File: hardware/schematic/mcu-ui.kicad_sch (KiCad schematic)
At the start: 25 parts, among them Q5 N MOSFET, SW1 TACT-SW, SW2 TACT-SW, U1 TCA9535, U4 ESP32-C3, U5 ST7567-12864, U6 EC11, U7 Si5351A, X1 32.768kHz-DNP

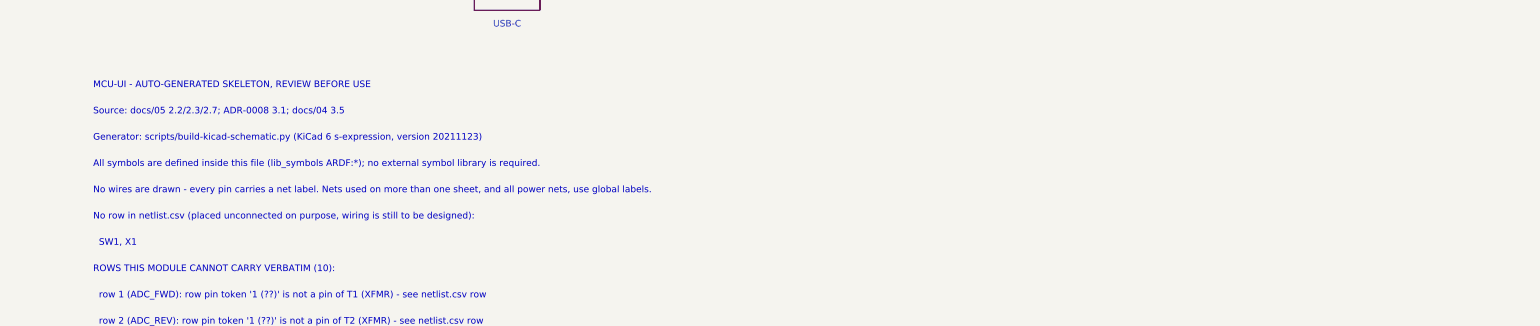
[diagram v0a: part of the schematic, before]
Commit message: docs(hw): BOM/网表生成器数据向 docs/05 同步（取消蜂鸣器 · R_BL2=100kΩ · CA-DV8008N@0x28）
前提修正: 「7 个 CSV 过期」不成立 —— 重跑后 6 个 BOM CSV + 2 个 netlist CSV
  **逐字节不变**；只有 schematic/netlist.md 变（相对 HEAD 145→123 行）
  ⇒ 真问题是「**生成器数据与 docs/05 不一致**」，重跑修不好 ⇒ 已在 3 个生成器里同步（无设计改动）

四条一致性（均已 grep 核实）:
  1. **蜂鸣器**: LS1 从「有源蜂鸣器 1 个」⇒ **本版移除 / 数量 0**; 外壳面板行同步删掉「出声孔」
  2. **R_BL2**: 10 kΩ ⇒ **100 kΩ**（BOM + netlist.md 备注）
  3. **CA-DV8008N @ 0x28**: HEAD 是 TCA9535(0x20)+ULN2003A+12V+继电器 12V 旧链
     → 现为 **U1 CA-DV8008N C54557228 / 0x28 / OC1-OC6→K1-K6 / COM→+5V / VCC→+3V3_DIG / A0-A2→GND**
     netlist 旧链 20 行只剩 1 行历史备注
  4. relay-wiring CHANGELOG 与派生文件一致（器件/地址/COM/线圈/映射/R_RLY 删除）

脚本重跑:
  · build-netlist.py → rc=0（3 产物, 155 行 / 68 nets）
  · build-lceda-import-pack.py → rc=0（9 模块 CSV + summary + bom.md）
  · **build-kicad-schematic.py → rc=1**（阻塞: netlist refs with no symbol/sheet: ['VCC','J17']）
  · check-kicad-schematic.py → **rc=1**（row coverage 181 vs netlist.csv 155）

⚠️ 未解决（已如实登记, 需设计层处理）:
  a. **KiCad 全套仍是 9/26 骨架**（含 TCA9535 / ULN2003A / U11 升压 / +12V / PA_PWR_PWM / R_RLY）
     → 需「**骨架移植**」, 重跑无法解决。**本次一个 .kicad_sch 都没写（未伪造）**, 自检器 FAIL 即为证据
  b. **GPIO 重分配未传播到生成器**（EC11_A→GPIO20 / LCD_BL→GPIO21 / GPIO12→示波器 / GPIO2→ADC1_CH2）
     生成器仍写 EC11_A=GPIO2、GPIO12_TBD、LCD_BL_DRV=TBD ⇒ 属设计数据重写（≈8 行+覆盖表）, 超出本次授权范围
  c. Q5/R_BL 的「驱动源待定」同 b（应为 GPIO21）
  d. mcu-ui.kicad_sch + kicad-build-report.md 的 10/15 改动来源不明（其余 7 份仍 9/26）

涉及: 20 个文档 .md · 3 个生成器脚本（数据同步, 无设计改动）· 11 个派生文件
  · 3 个新增: docs/adr/ADR-0009-atu-4c2l-series-c-shunt-l.md
    hardware/antenna/test/2026-10-field-measurements.md · hardware/antenna/test/impedance-table.md

未烧录/未做任何 git checkout/stash/clean（不丢任何人的改动）。
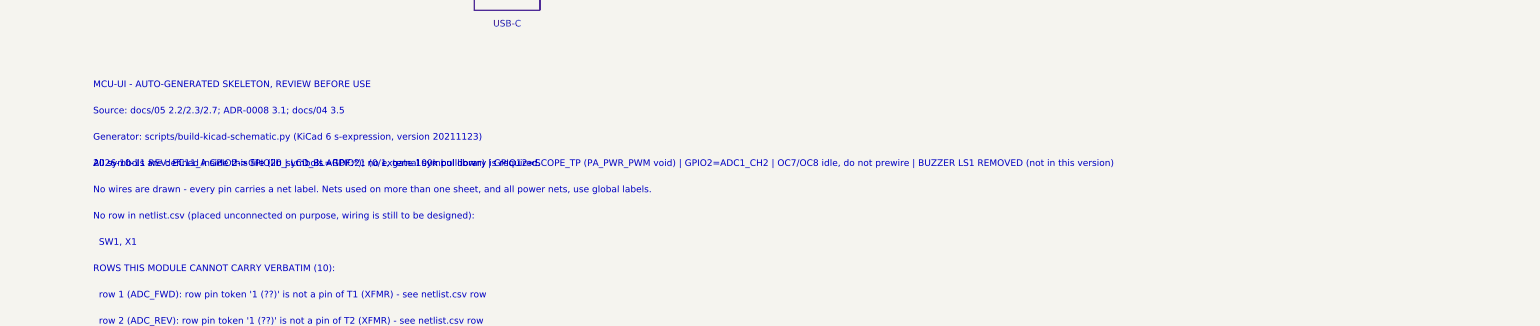
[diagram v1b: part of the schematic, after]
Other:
- note added: "2026-10-11 REV: EC11_A GPIO2->GPIO20 | LCD_BL=GPIO21 (0/1, gate 100k pulldown) | GPIO12=SCOPE_TP (PA_PWR_PWM void) | GPIO2=ADC1_CH2 | OC7/OC8 idle, do not prewire | BUZZER LS1 REMOVED (not in this version)"
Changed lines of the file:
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@@
       "Auto-generated skeleton - see hardware/schematic/IMPORT-TO-LCEDA.md"
+    )
+    (comment 2
+      "2026-10-11: EC11_A=GPIO20 LCD_BL=GPIO21 SCOPE_TP=GPIO12 ADC1_CH2=GPIO2; OC7/OC8 idle; BUZZER LS1 NOT IN THIS VERSION"
     )
   )
@@
     (effects (font (size 1.27 1.27)) (justify left bottom))
   )
+  (text "2026-10-11 REV: EC11_A GPIO2->GPIO20 | LCD_BL=GPIO21 (0/1, gate 100k pulldown) | GPIO12=SCOPE_TP (PA_PWR_PWM void) | GPIO2=ADC1_CH2 | OC7/OC8 idle, do not prewire | BUZZER LS1 REMOVED (not in this version)"
+    (at 15.24 162.56 0)
+    (effects (font (size 1.27 1.27)) (justify left bottom))
+  )
